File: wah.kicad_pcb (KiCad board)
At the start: 4 copper layers, 99.1 x 54.5 mm, 38 parts, among them J1 Barrel_Jack_Switch, J2 In, J3 Out, SW1 SW_Push_3PDT, U1 TL072, U2 L78L05_TO92

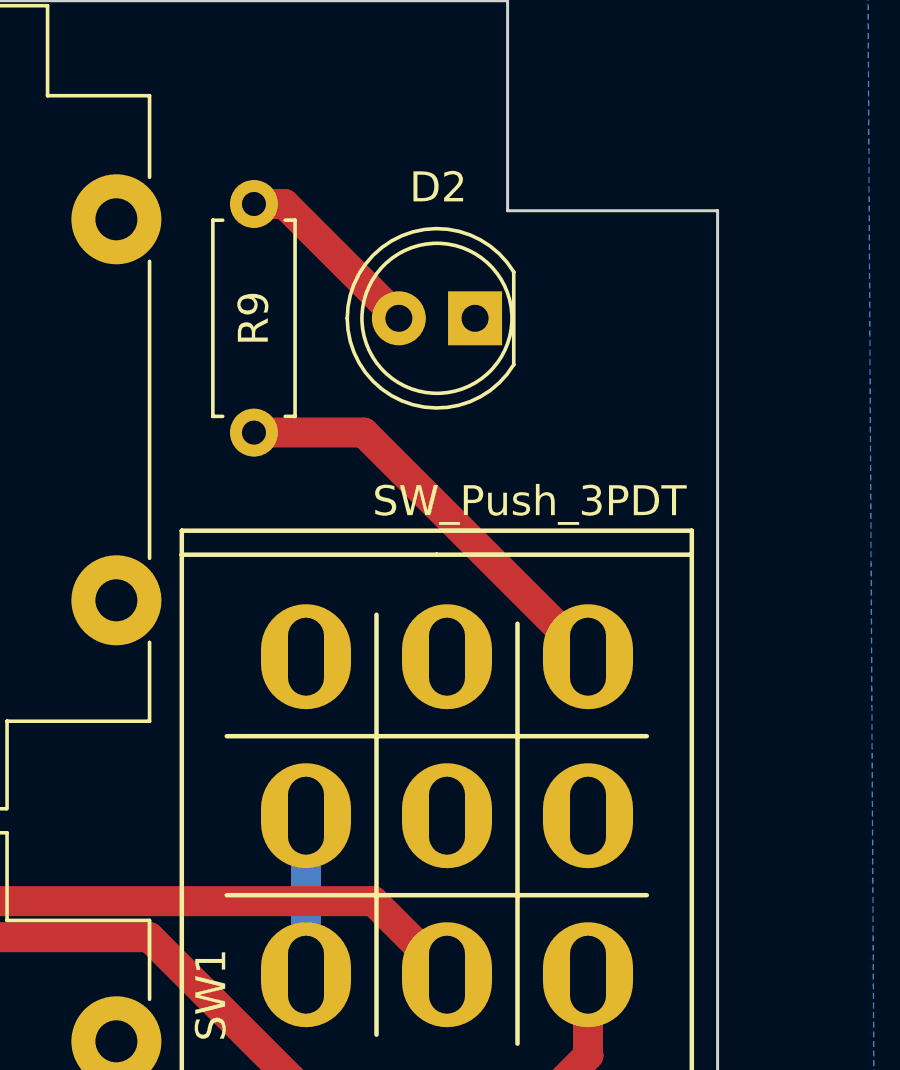
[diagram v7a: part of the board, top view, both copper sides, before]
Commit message: move LED resistor
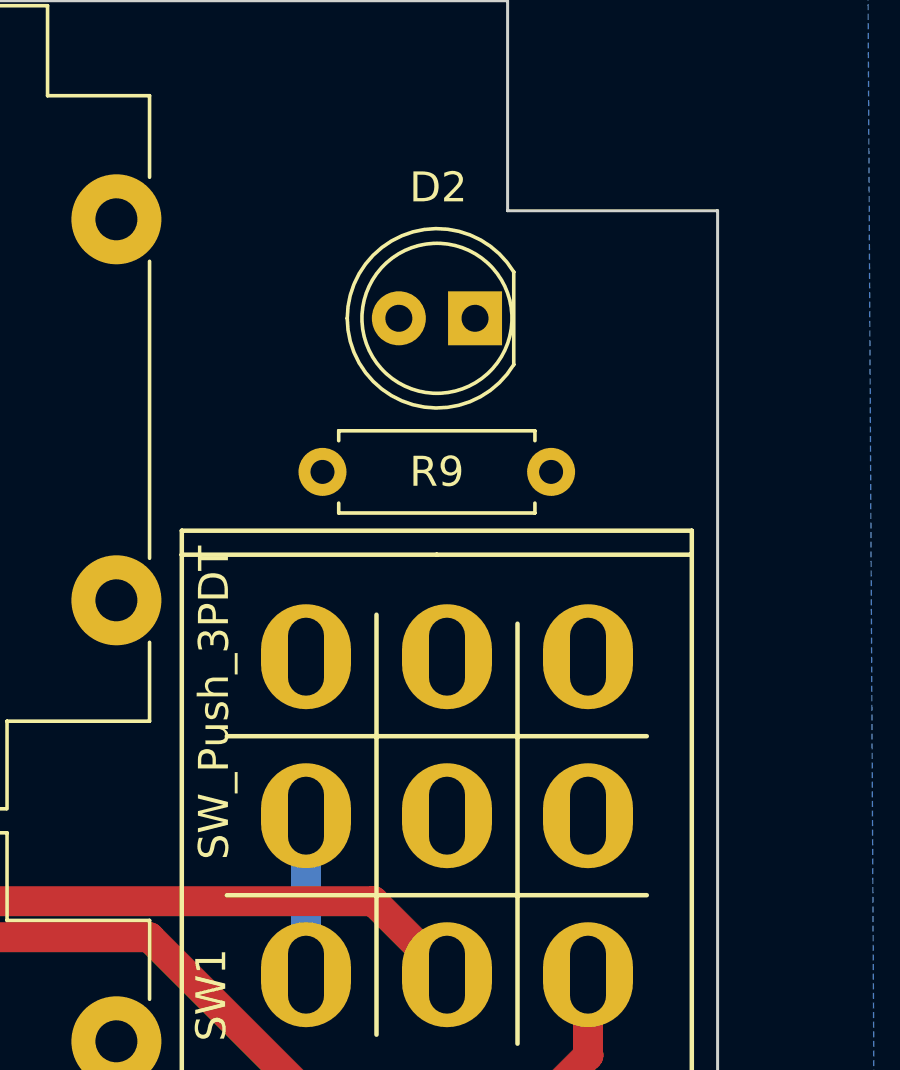
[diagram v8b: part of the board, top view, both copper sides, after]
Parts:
- moved R9 9.99 mm to (136.0, 48.9), turned to 180 degrees
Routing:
- net Net-(R9-Pad1): track 14.2 -> 6.67 mm
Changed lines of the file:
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@@
 	(title_block
 		(title "Wah")
-		(date "2025-11-10")
-		(rev "0.4.2")
+		(date "2025-11-11")
+		(rev "0.4.3")
 		(company "KnightHill Engineering")
 	)
@@
 	(footprint "Resistor_THT:R_Axial_DIN0207_L6.3mm_D2.5mm_P7.62mm_Horizontal"
 		(layer "F.Cu")
-		(at 126.1 47.58 90)
+		(at 136.005 48.89 180)
 		(descr "Resistor, Axial_DIN0207 series, Axial, Horizontal, pin pitch=7.62mm, 0.25W = 1/4W, length*diameter=6.3*2.5mm^2, http://cdn-reichelt.de/documents/datenblatt/B400/1_4W%23YAG.pdf")
 		(tags "Resistor Axial_DIN0207 series Axial Horizontal pin pitch 7.62mm 0.25W = 1/4W length 6.3mm diameter 2.5mm")
 		(property "Reference" "R9"
-			(at 3.81 0 90)
+			(at 3.81 0 0)
 			(layer "F.SilkS")
 			(effects
@@
 		)
 		(property "Value" "R"
-			(at 3.81 2.37 90)
+			(at 3.81 2.37 0)
 			(layer "F.Fab")
 			(effects
@@
 		)
 		(property "Datasheet" "~"
-			(at 0 0 90)
+			(at 0 0 0)
 			(layer "F.Fab")
 			(hide yes)
@@
 		)
 		(property "Description" "Resistor"
-			(at 0 0 90)
+			(at 0 0 0)
 			(layer "F.Fab")
 			(hide yes)
@@
 		(attr through_hole exclude_from_pos_files)
 		(fp_line
-			(start 7.08 -1.37)
-			(end 7.08 -1.04)
+			(start 7.08 1.37)
+			(end 7.08 1.04)
 			(stroke
 				(width 0.12)
@@
 		)
 		(fp_line
-			(start 0.54 -1.37)
-			(end 7.08 -1.37)
+			(start 7.08 -1.37)
+			(end 7.08 -1.04)
 			(stroke
 				(width 0.12)
@@
 		)
 		(fp_line
-			(start 0.54 -1.04)
-			(end 0.54 -1.37)
+			(start 0.54 1.37)
+			(end 7.08 1.37)
 			(stroke
 				(width 0.12)
@@
 		)
 		(fp_line
-			(start 7.08 1.37)
-			(end 7.08 1.04)
+			(start 0.54 -1.04)
+			(end 0.54 -1.37)
 			(stroke
 				(width 0.12)
@@
 		)
 		(fp_line
-			(start 0.54 1.37)
-			(end 7.08 1.37)
+			(start 0.54 -1.37)
+			(end 7.08 -1.37)
 			(stroke
 				(width 0.12)
@@
 		)
 		(fp_text user "${REFERENCE}"
-			(at 3.81 0 90)
+			(at 3.81 0 0)
 			(layer "F.Fab")
 			(effects
@@
 		)
 		(pad "1" thru_hole circle
-			(at 0 0 90)
+			(at 0 0 180)
 			(size 1.6 1.6)
 			(drill 0.8)
@@
 		)
 		(pad "2" thru_hole circle
-			(at 7.62 0 90)
+			(at 7.62 0 180)
 			(size 1.6 1.6)
 			(drill 0.8)
@@
 		)
 		(property "Value" "SW_Push_3PDT"
-			(at 10.78 3.09 180)
+			(at 4.065 -7.425 270)
 			(layer "F.SilkS")
 			(effects
@@
 	)
 	(segment
-		(start 127.12 39.96)
-		(end 130.93 43.77)
-		(width 1)
-		(layer "F.Cu")
+		(start 128.385 46.315)
+		(end 128.385 48.89)
+		(width 0.5)
+		(layer "In1.Cu")
 		(net 33)
 	)
 	(segment
-		(start 126.1 39.96)
-		(end 127.12 39.96)
-		(width 1)
-		(layer "F.Cu")
+		(start 130.93 43.77)
+		(end 128.385 46.315)
+		(width 0.5)
+		(layer "In1.Cu")
 		(net 33)
 	)
@@
 	)
 	(segment
-		(start 129.765 47.58)
-		(end 137.235 55.05)
-		(width 1)
-		(layer "F.Cu")
+		(start 137.235 50.12)
+		(end 136.005 48.89)
+		(width 0.5)
+		(layer "In1.Cu")
 		(net 54)
 	)
 	(segment
-		(start 126.1 47.58)
-		(end 129.765 47.58)
-		(width 1)
-		(layer "F.Cu")
+		(start 137.235 55.05)
+		(end 137.235 50.12)
+		(width 0.5)
+		(layer "In1.Cu")
 		(net 54)
 	)
